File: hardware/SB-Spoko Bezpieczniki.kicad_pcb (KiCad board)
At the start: 4 copper layers, 179 x 60 mm, 148 parts, among them IC1 STM32L4P5RET6, J1 SWD, Q1 Q_NMOS_DGS, Q2 Q_NMOS_DGS, Q3 Q_NMOS_DGS, Q4 Q_NMOS_DGS, Q5 Q_NMOS_DGS, SW1 RESET, U1 AS222-35PN-933, U10 VOH1016AB-T2, U11 ATA6561-GAQW-N, U12 SMART FUSE, U13 SMART FUSE, U14 SMART FUSE, U15 SMART FUSE, U16 MCP14A0052T, U17 MCP14A0052T, U18 MCP14A0052T, U2 LM2596S-12, U3 LM2596S-5, U4 LP2950-3.3_TO92, U5 VOH1016AB-T2, U6 VOH1016AB-T2, U7 VOH1016AB-T2, U8 VOH1016AB-T2, U9 VOH1016AB-T2, Y1 THE_CLOCK

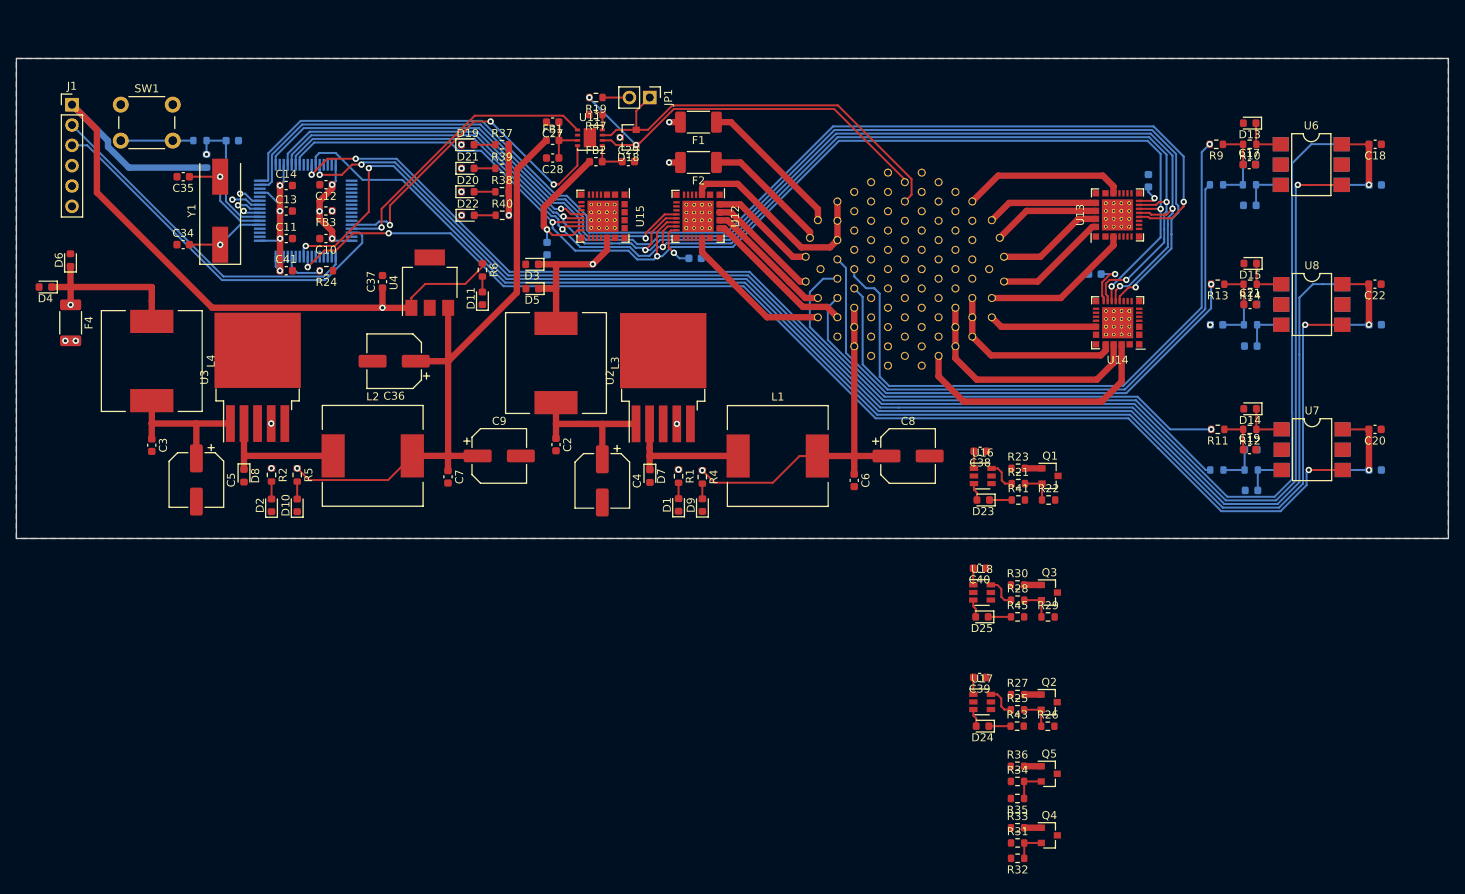
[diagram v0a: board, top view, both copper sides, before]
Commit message: 1. added 2X20 connector, \n 2. changed the footprints of schootkies and zenner diodes to a bigger ones, \n 3. changed pcb layout entirely couse duck me, that connector i too duking BIG.
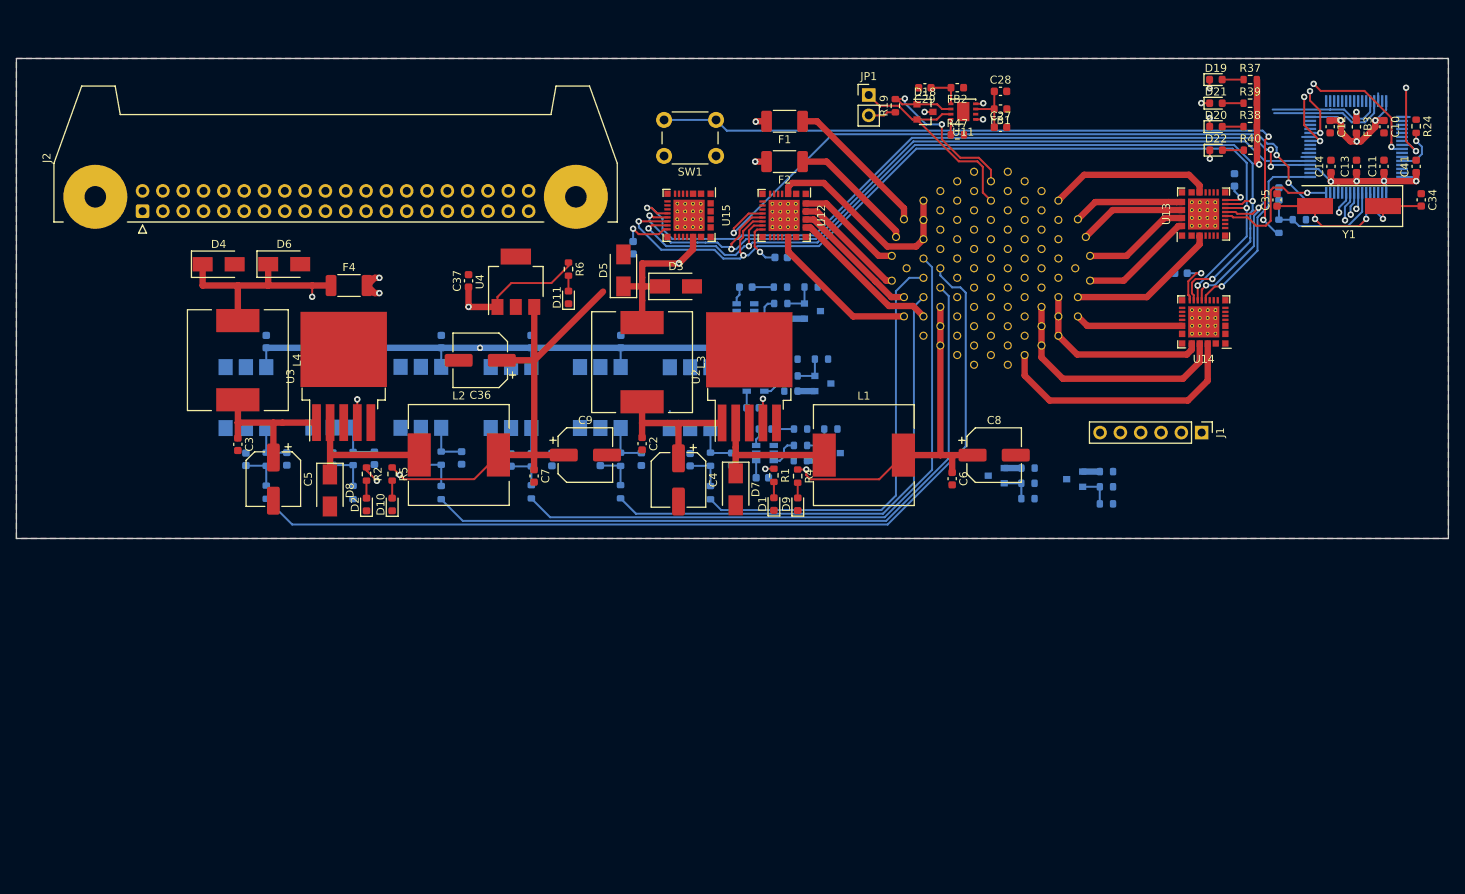
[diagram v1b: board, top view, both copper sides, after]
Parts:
- added J2: Conn_02x20_Odd_Even, Connector_IDC:IDC-Header_2x20-1MP_P2.54mm_Latch_Horizontal, F.Cu at (86.8, 89.1)
- C17, C18, C19, C20, C21, C22, C38, C39, C40, D13, D14, D15, D23, D24, D25, Q1, Q2, Q3, Q4, Q5, R10, R11, R12, R13, R14, R21, R22, R23, R25, R26, R27, R28, R29, R30, R31, R32, R33, R34, R35, R36, R41, R43, R45, R9, U16, U17, U18, U6, U7, U8: moved to B.Cu
- D3, D4, D5, D6, D7, D8: footprint Diode_SMD:D_0603_1608Metric -> Diode_SMD:D_SMA
- moved C34 154.9 mm to (246.6, 87.7), turned to 270 degrees
- moved J1 147.0 mm to (219.2, 116.8), turned to 270 degrees
- moved C41 141.8 mm to (246.0, 83.5), turned to 90 degrees
- moved Y1 141.1 mm to (237.6, 88.5), turned to 180 degrees
- moved C16 140.0 mm to (102.2, 105.4), turned to 270 degrees
- moved C11 137.5 mm to (241.9, 83.5), turned to 90 degrees
- moved R24 137.4 mm to (246.0, 78.5), turned to 270 degrees
- moved R3 136.8 mm to (231.4, 90.2), turned to 180 degrees
- moved C35 136.8 mm to (228.6, 87.7), turned to 90 degrees
- moved U5 136.3 mm to (99.7, 112.4), turned to 90 degrees
- moved R20 135.3 mm to (228.8, 91.0), turned to 90 degrees
- moved C13 133.9 mm to (238.5, 83.5), turned to 90 degrees
- moved C10 133.0 mm to (241.9, 78.5), turned to 270 degrees
- moved IC1 131.6 mm to (238.5, 81.1), turned to 90 degrees
- moved C33 131.0 mm to (228.8, 86.9), turned to 90 degrees
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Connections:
- net /CAN_H renamed /CAR_CAN+
- net /CAN_L renamed /CAR_CAN-
- net Net-(U1-Pad35) renamed /INV_CAN+
- net Net-(U1-Pad36) renamed /INV_CAN-
- IC1 pad 10: /STM_SOFT_ERROR -> /STM_FATAL_ERROR
- IC1 pad 11: /STM_OK -> /STM_???
- IC1 pad 8: /STM_??? -> /STM_OK
- IC1 pad 9: /STM_FATAL_ERROR -> /STM_SOFT_ERROR
- U1 pad 81: /HVD -> /TSMS
- U1 pad 82: /TSMS -> /SPARE
- U1 pad 89: /TD -> /AMS
- U1 pad 90: /SPARE -> /HVD
- U1 pad 91: /AMS -> /TD
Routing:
- net /N_TSMS: track 189.7 -> 7.57 mm
- net /N_HVD: track 185.0 -> 7.01 mm, vias 3 -> 2
- net /N_TD: track 168.8 -> 1.02 mm, vias 1 -> 0
- net /SAFETY: track 180.8 -> 16.6 mm
- net /N_AMS: track 149.9 -> 10.5 mm, vias 3 -> 2
- net /SS_1: track 146.9 -> 17.6 mm
- net /SS_2: track 151.4 -> 24.0 mm
- net +3V3: track 395.0 -> 289.4 mm, vias 10 -> 8
- net Net-(R20-Pad1): track 9.02 -> 89.8 mm, vias 0 -> 2
- net /SS_3: track 43.5 -> 96.2 mm, vias 1 -> 3
- net /SWDIO: track 47.6 -> 0.97 mm
- net /TSMS: track 74.0 -> 117.0 mm
- net /SWCLK: track 42.4 -> 0.97 mm
- net /MISO: track 157.2 -> 116.2 mm
- net /MOSI: track 155.9 -> 118.1 mm
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
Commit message: Updated to be compatible with KiCad 6.0.0, changed chematics layouts to fit in A4 worksheet and finished routing the rest of the signals.
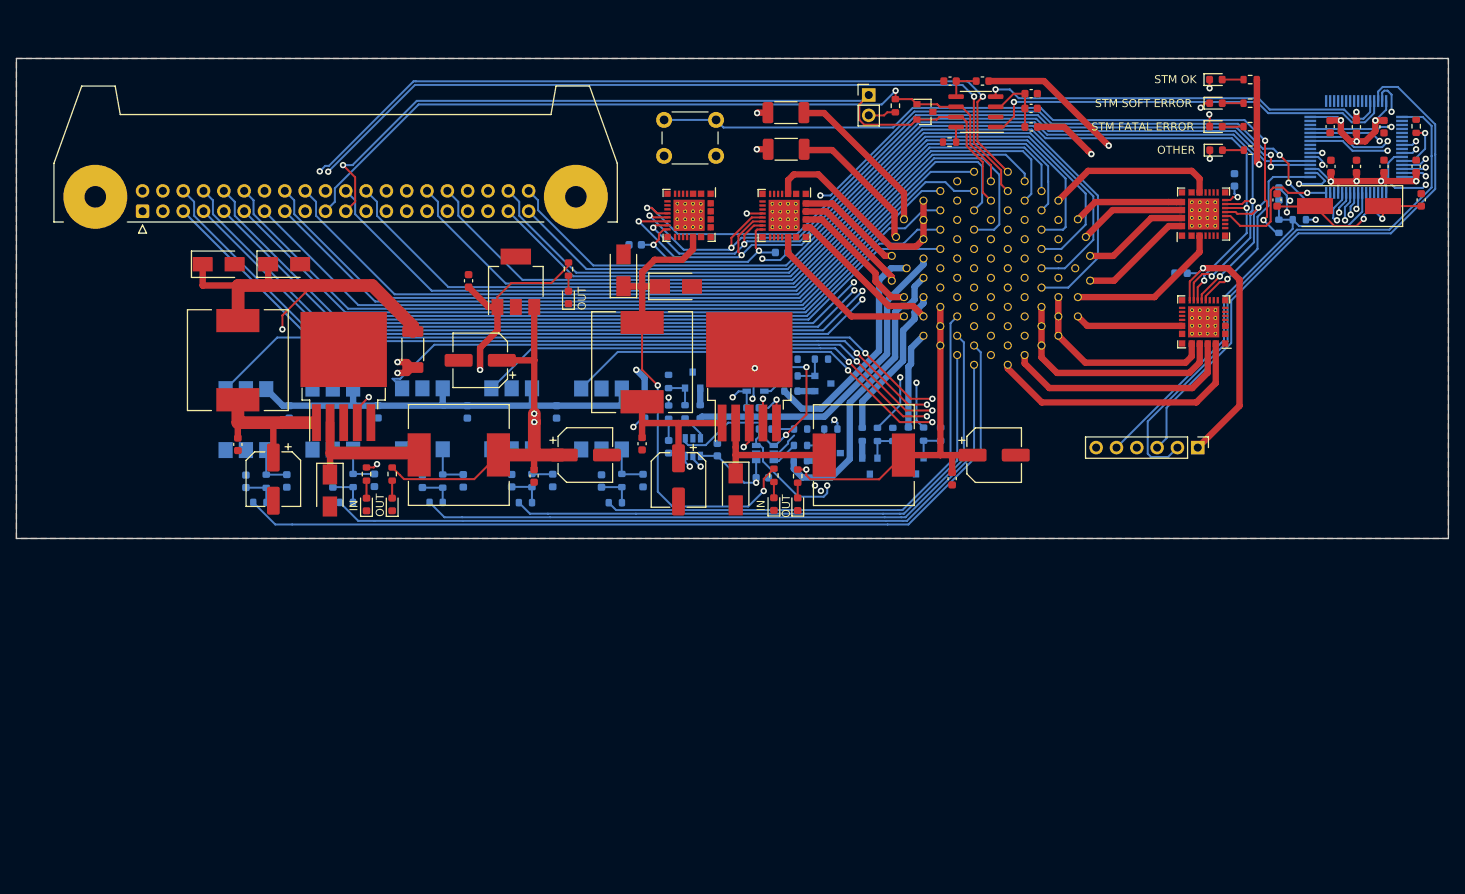
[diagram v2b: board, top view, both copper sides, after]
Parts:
- removed C25: 10nF, Capacitor_SMD:C_0603_1608Metric
- removed C26: 100nF, Capacitor_SMD:C_0603_1608Metric
- removed D17: D_SCH, Diode_SMD:D_0603_1608Metric
- removed R17, R18: 4k7, Resistor_SMD:R_0603_1608Metric
- removed U10: VOH1016AB-T2, Package_DIP:SMDIP-6_W7.62mm
- U11: value ATA6561-GAQW-N -> MCP2558FD-xSN; footprint Package_DFN_QFN:DFN-8-1EP_3x3mm_P0.65mm_EP1.55x2.4mm -> Package_SO:SOIC-8_3.9x4.9mm_P1.27mm
- moved R36 25.2 mm to (182.5, 117.0), turned to -90 degrees
- moved R34 23.8 mm to (184.4, 117.0), turned to -90 degrees
- moved R35 22.5 mm to (186.5, 117.0), turned to 90 degrees
- moved D24 22.2 mm to (152.5, 118.5), turned to -90 degrees
- moved R26 21.4 mm to (152.5, 110.4), turned to 90 degrees
- moved R33 21.1 mm to (176.7, 117.0), turned to -90 degrees
- moved R43 21.0 mm to (152.5, 114.2), turned to 90 degrees
- moved Q5 19.9 mm to (183.4, 120.9), turned to -90 degrees
- moved R31 19.8 mm to (178.6, 117.0), turned to -90 degrees
- moved R32 18.7 mm to (180.6, 117.0), turned to 90 degrees
- moved U17 18.2 mm to (155.6, 118.6), turned to 90 degrees
- moved R25 18.1 mm to (154.6, 114.2), turned to 90 degrees
- moved Q2 17.3 mm to (155.5, 110.2), turned to 90 degrees
- moved Q4 15.8 mm to (177.7, 121.0), turned to -90 degrees
- moved R27 15.4 mm to (156.5, 114.2), turned to 90 degrees
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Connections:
- net /3.3V_STM_POWER renamed 3.3V_STM_POWER
- net /APPS renamed APPS
- net /BOXF_MB renamed BOXF_MB
- net /BOX_DV renamed BOX_DV
- net /BUZZER_CONTROL renamed BUZZER_CONTROL
- net /BUZZER_CRL_OUT renamed BUZZER_CRL_OUT
- net /CAN_RX renamed CAN_RX
- net /CAN_TX renamed CAN_TX
- net /CONVERT_5V renamed CONVERT_5V
- net /DASHBOARD renamed DASHBOARD
- net /FAN_L renamed FAN_L
- net /FAN_R renamed FAN_R
- net /INTEL_NUC renamed INTEL_NUC
- net /INVERTER renamed INVERTER
- net /JETSON_??? renamed JETSON_???
- net /LED_1_CONTROL renamed LED_1_CONTROL
- net /LED_1_CRL_OUT renamed LED_1_CRL_OUT
- net /LED_2_CONTROL renamed LED_2_CONTROL
- net /LED_2_CRL_OUT renamed LED_2_CRL_OUT
- net /MISO renamed MISO
- net /MOSI renamed MOSI
- net /N_RST renamed N_RST
- net /PUMP renamed PUMP
- net /SCK renamed SCK
- net /SS_0 renamed SS_0
- net /SS_1 renamed SS_1
- net /SS_2 renamed SS_2
- net /SS_3 renamed SS_3
- net /STM_??? renamed STM_???
- net /STM_CKL_OUT renamed STM_CKL_OUT
- net /STM_CLK_IN renamed STM_CLK_IN
- net /STM_FATAL_ERROR renamed STM_FATAL_ERROR
- net /STM_OK renamed STM_OK
- net /STM_SOFT_ERROR renamed STM_SOFT_ERROR
- net /SWCLK renamed SWCLK
- net /SWDIO renamed SWDIO
- net /TSAL_HV renamed TSAL_HV
- net /TSAL_LOGIC renamed TSAL_LOGIC
- net /V_BSPD renamed V_BSPD
- net /V_EBS renamed V_EBS
- net /V_PUMP renamed V_PUMP
- net /WHEEL renamed WHEEL
- net /WS_FL renamed WS_FL
- net /WS_FR renamed WS_FR
- net /WS_RL renamed WS_RL
- net /WS_RR renamed WS_RR
- D18 pad 1: /CAR_CAN+ -> CAR_CAN+
- D18 pad 2: /CAR_CAN- -> CAR_CAN-
- IC1 pad 26: /N_TSMS -> N_AMS
- IC1 pad 27: /N_TD -> N_SPARE
- IC1 pad 28: /N_HVD -> N_TSMS
- IC1 pad 56: /N_AMS -> N_TD
- IC1 pad 57: /SAFETY -> Net-(IC1-Pad57)
- IC1 pad 58: /N_SPARE -> N_HVD
- IC1 pad 62: Net-(IC1-Pad62) -> EN_MOSFET
- J2 pad 1: Net-(J2-Pad1) -> +5V
- J2 pad 10: Net-(J2-Pad10) -> WATER_NTC_2
- J2 pad 11: Net-(J2-Pad11) -> RES_SIN-
- J2 pad 12: Net-(J2-Pad12) -> WATER_NTC_1
- J2 pad 13: Net-(J2-Pad13) -> RES_COS+
- J2 pad 14: Net-(J2-Pad14) -> GND
- J2 pad 15: Net-(J2-Pad15) -> RES_COS-
- J2 pad 16: Net-(J2-Pad16) -> SP_L-
- J2 pad 17: Net-(J2-Pad17) -> GND
- J2 pad 18: Net-(J2-Pad18) -> SP_L+
- J2 pad 19: Net-(J2-Pad19) -> CAR_CAN+
- J2 pad 2: Net-(J2-Pad2) -> +5V
- J2 pad 20: Net-(J2-Pad20) -> GND
- J2 pad 21: Net-(J2-Pad21) -> CAR_CAN-
- J2 pad 22: Net-(J2-Pad22) -> USB_DEBUG_DP
- J2 pad 23: Net-(J2-Pad23) -> INV_CAN+
- J2 pad 24: Net-(J2-Pad24) -> USB_DEBUG_DM
- J2 pad 25: Net-(J2-Pad25) -> INV_CAN-
- J2 pad 3: Net-(J2-Pad3) -> GND
- J2 pad 30: Net-(J2-Pad30) -> USB_DP
- J2 pad 31: Net-(J2-Pad31) -> GND
- J2 pad 32: Net-(J2-Pad32) -> USB_DM
- J2 pad 33: Net-(J2-Pad33) -> BREAK_LIGHT_GATE
- J2 pad 34: Net-(J2-Pad34) -> GND
- J2 pad 35: Net-(J2-Pad35) -> RTDS_GATE
- J2 pad 37: Net-(J2-Pad37) -> WSS_RL
- J2 pad 38: Net-(J2-Pad38) -> WSS_FL
- J2 pad 39: Net-(J2-Pad39) -> WSS_RR
- J2 pad 4: Net-(J2-Pad4) -> GND
- J2 pad 40: Net-(J2-Pad40) -> WSS_FR
- J2 pad 5: Net-(J2-Pad5) -> RES_REF+
- J2 pad 6: Net-(J2-Pad6) -> WATER_P
- J2 pad 7: Net-(J2-Pad7) -> RES_REF-
- J2 pad 8: Net-(J2-Pad8) -> MONO_NTC
- J2 pad 9: Net-(J2-Pad9) -> RES_SIN+
- JP1 pad 1: /CAR_CAN- -> CAR_CAN-
- R11 pad 2: /AMS -> AMS
- R13 pad 2: /TD -> TD
- R15 pad 2: +24V -> SPARE
- R19 pad 2: /CAR_CAN+ -> CAR_CAN+
- R23 pad 1: /BUZZER_IN -> BUZZER_IN
- R27 pad 1: /LED_2_IN -> LED_2_IN
- R30 pad 1: /LED_1_IN -> LED_1_IN
- R31 pad 1: /RTDS_GATE -> RTDS_GATE
- R33 pad 1: /RTDS_IN -> RTDS_IN
- R34 pad 1: /BREAK_LIGHT_GATE -> BREAK_LIGHT_GATE
- R36 pad 1: /BREAK_LIGHT_IN -> BREAK_LIGHT_IN
- R7 pad 2: /TSMS -> TSMS
- R9 pad 2: /HVD -> HVD
- U1 pad 10: /LED_2_IN -> Net-(U1-Pad10)
- U1 pad 11: /LED_1_IN -> Net-(U1-Pad11)
- U1 pad 12: /RTDS_IN -> Net-(U1-Pad12)
- U1 pad 16: Net-(U1-Pad16) -> USB_DP
- U1 pad 17: Net-(U1-Pad17) -> USB_DM
- U1 pad 18: Net-(U1-Pad18) -> WSS_RL
- U1 pad 19: Net-(U1-Pad19) -> WSS_FL
- U1 pad 20: Net-(U1-Pad20) -> WSS_RR
- U1 pad 21: Net-(U1-Pad21) -> WSS_FR
- U1 pad 25: Net-(U1-Pad25) -> USB_DEBUG_DP
- U1 pad 26: Net-(U1-Pad26) -> USB_DEBUG_DM
- U1 pad 35: /INV_CAN+ -> INV_CAN+
- U1 pad 36: /INV_CAN- -> INV_CAN-
- U1 pad 4: /BREAK_LIGHT_IN -> Net-(U1-Pad4)
- U1 pad 45: Net-(U1-Pad45) -> V_SAFETY
- U1 pad 46: /CAR_CAN+ -> CAR_CAN+
- U1 pad 47: /CAR_CAN- -> CAR_CAN-
- U1 pad 56: Net-(U1-Pad56) -> RES_COS-
- U1 pad 57: Net-(U1-Pad57) -> RES_COS+
- U1 pad 58: Net-(U1-Pad58) -> SP_L-
- U1 pad 59: Net-(U1-Pad59) -> SP_L+
- U1 pad 65: Net-(U1-Pad65) -> TSMS
- U1 pad 66: Net-(U1-Pad66) -> SPARE
- U1 pad 67: Net-(U1-Pad67) -> MONO_NTC
- U1 pad 68: Net-(U1-Pad68) -> RES_REF-
- U1 pad 69: Net-(U1-Pad69) -> WATER_P
- U1 pad 70: Net-(U1-Pad70) -> RES_REF+
- U1 pad 74: Net-(U1-Pad74) -> HVD
- U1 pad 75: Net-(U1-Pad75) -> AMS
- U1 pad 76: Net-(U1-Pad76) -> TD
- U1 pad 77: Net-(U1-Pad77) -> WATER_NTC_1
- U1 pad 78: Net-(U1-Pad78) -> RES_SIN-
- U1 pad 79: Net-(U1-Pad79) -> WATER_NTC_2
- U1 pad 80: Net-(U1-Pad80) -> RES_SIN+
- U1 pad 81: /TSMS -> Net-(U1-Pad81)
- U1 pad 82: /SPARE -> Net-(U1-Pad82)
- U1 pad 89: /AMS -> LED_2_IN
- U1 pad 9: /BUZZER_IN -> Net-(U1-Pad9)
- U1 pad 90: /HVD -> BUZZER_IN
- U1 pad 91: /TD -> RTDS_IN
- U1 pad 93: Net-(U1-Pad93) -> BREAK_LIGHT_IN
- U1 pad 97: Net-(U1-Pad97) -> LED_1_IN
- U11 pad 6: /CAR_CAN+ -> CAR_CAN+
- U11 pad 7: /CAR_CAN- -> CAR_CAN-
- U14 pad 31: /Fuse 2/VOUT_1 -> V_SAFETY
- U14 pad 32: /Fuse 2/VOUT_1 -> V_SAFETY
- U16 pad 4: /EN_MOSFET -> EN_MOSFET
- U17 pad 4: /EN_MOSFET -> EN_MOSFET
- U18 pad 4: /EN_MOSFET -> EN_MOSFET
- U5 pad 4: /N_TSMS -> N_TSMS
- U6 pad 4: /N_HVD -> N_HVD
- U7 pad 4: /N_AMS -> N_AMS
- U8 pad 4: /N_TD -> N_TD
- U9 pad 4: /SAFETY -> N_SPARE
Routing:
- net +5V: track 82.7 -> 277.8 mm, vias 2 -> 6
- net N_TSMS: track 0.00 -> 180.2 mm, vias 0 -> 3
- net N_SPARE: track 0.00 -> 171.8 mm, vias 0 -> 3
- net N_AMS: track 0.00 -> 161.7 mm, vias 0 -> 3
- net N_TD: track 0.00 -> 142.4 mm, vias 0 -> 3
- net EN_MOSFET: track 0.00 -> 132.6 mm, vias 0 -> 3
- net N_HVD: track 0.00 -> 130.8 mm, vias 0 -> 3
- net BUZZER_CONTROL: track 2.21 -> 132.6 mm, vias 0 -> 2
- net LED_2_CONTROL: track 2.23 -> 125.7 mm, vias 0 -> 3
- net LED_1_CONTROL: track 2.23 -> 124.5 mm, vias 0 -> 3
- net /TSMS: track 117.0 -> 0.00 mm
- net WATER_P: track 0.00 -> 113.6 mm, vias 0 -> 1
- net MONO_NTC: track 0.00 -> 111.5 mm, vias 0 -> 1
- net RES_REF+: track 0.00 -> 110.8 mm, vias 0 -> 1
- net SP_L+: track 0.00 -> 110.7 mm
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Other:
- net class Default removed
- board text added: "IN"
- board text added: "OTHER"
- board text added: "OUT"
- board text added: "STM FATAL ERROR"
- board text added: "STM OK"
- board text added: "STM SOFT ERROR"
